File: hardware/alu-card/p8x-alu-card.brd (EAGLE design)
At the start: 160 x 100 mm, 77 parts, among them J1 FABC96R, U1 74HCT377, U10 74HCT181, U11 74HCT182, U12 74HCT157, U13 74HCT157, U14 74HCT157, U15 74HCT157, U16 74HCT244, U17 FLAGS, U18 74HCT260, U19 74HCT08, U2 74HCT244, U20 74HCT138, U21 74HCT138, U22 74HCT157, U23 74HCT244, U24 74HCT32, U25 74HCT00, U26 74HCT74, U27 74HCT260, U28 74HCT157, U29 74HCT157, U3 74HCT377, U30 74HCT157, U31 74HCT08, U32 74HCT157, U33 74HCT157, U34 74HCT86, U35 74HCT08, U4 74HCT244, U5 74HCT377, U6 74HCT244, U7 74HCT377, U8 74HCT244, U9 74HCT181

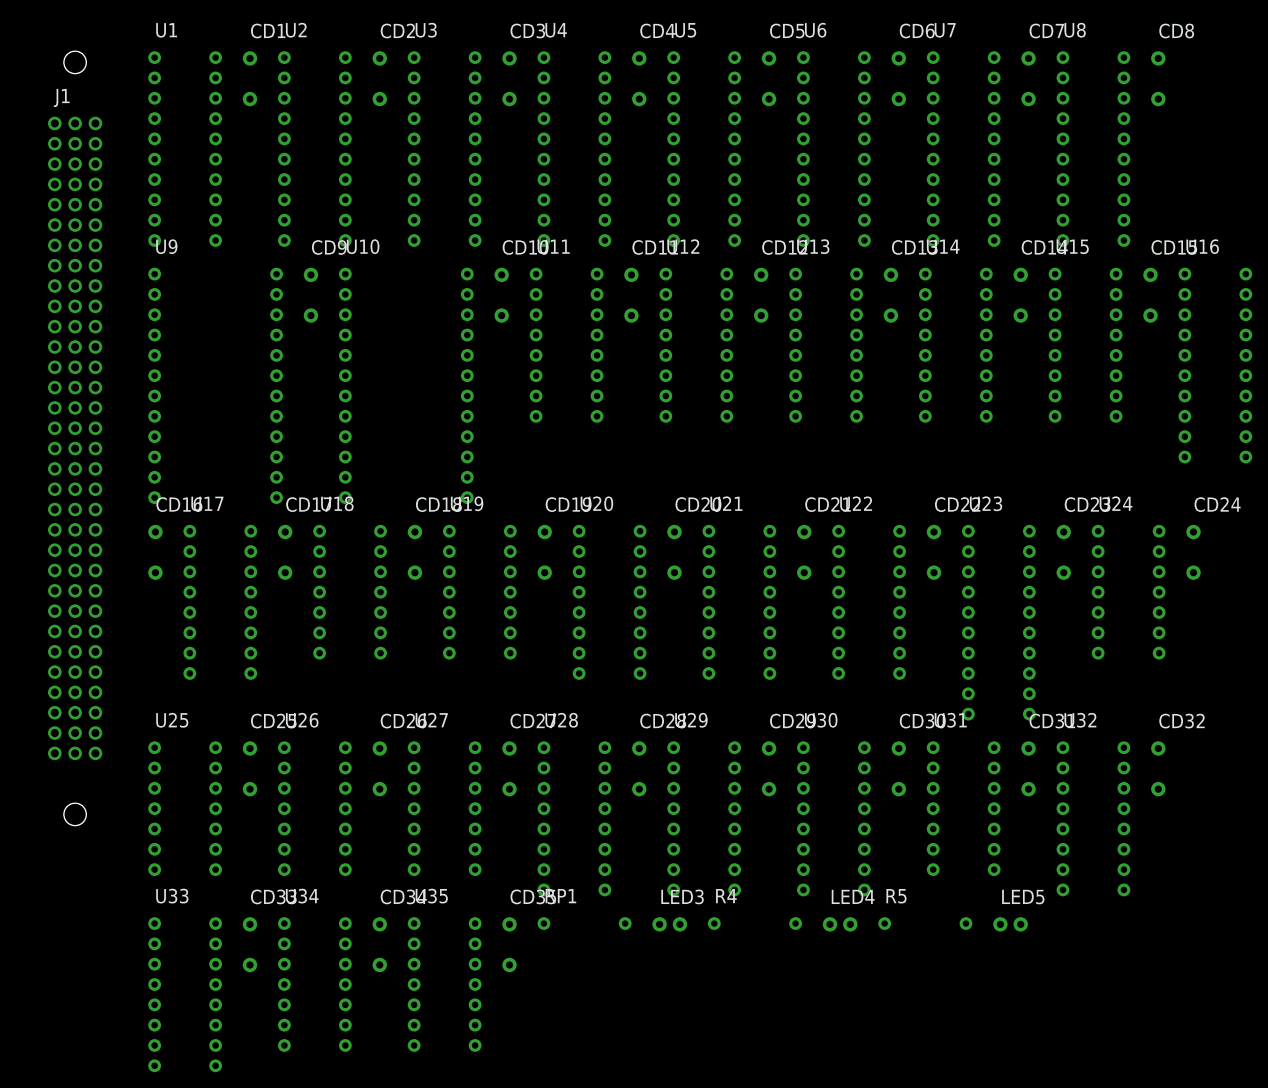
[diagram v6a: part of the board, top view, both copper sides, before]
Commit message: feat(hardware): use con-vg DIN 41612 footprints (MABC96R card / FABC96S backplane)
Replace the hand-rolled DIN96/DIN96C connector packages with the real Eagle
con-vg DIN 41612 footprints (geometry baked into the generator so it stays
self-contained): card edge = MABC96R (male right-angle), backplane = FABC96S
(female vertical) — both A/B/C @ 2.54mm, drill 0.9144, two M2.5 mounting holes
at y=+/-45. Card value -> MABC96R; pin->pad names unchanged (A1..C32) so the
netlist is intact.

con-vg centres the pad field on the element origin, so the backplane (hand-
placed/routed) was re-derived: slots dropped to y=54.6 to centre the pin field
on the 109mm board (pads now on-board), bus traces re-routed to the new A/B/C
columns (element at sx(i)-2.54). Cards auto-adapt via fp_box. All 8 boards
validate (0 errors).

Known: 3 placement-overlap WARNINGS on the backplane (power-LED resistor; CT2/RT1
clock terminators, both DNP) where the taller connector crowds the top/bottom
strips — to clear during the Fusion placement pass.

Co-Authored-By: Claude Opus 4.8 <noreply@anthropic.com>
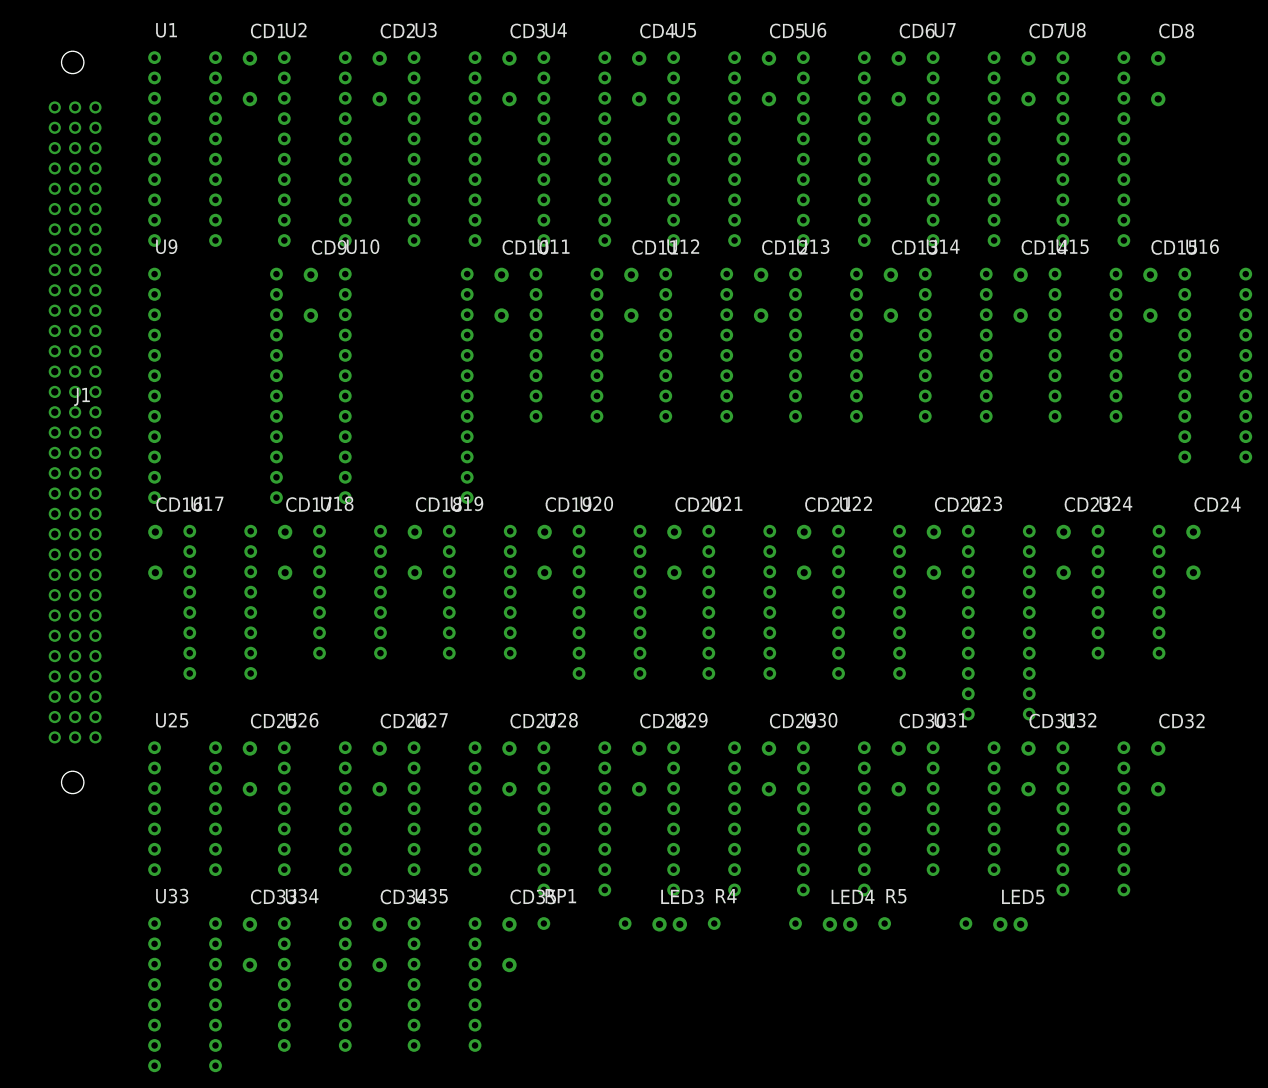
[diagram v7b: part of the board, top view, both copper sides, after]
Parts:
- J1: value FABC96R -> MABC96R; device p8x:DIN96C -> p8x:MABC96R
- moved J1 37.5 mm to (193.3, 49.6)

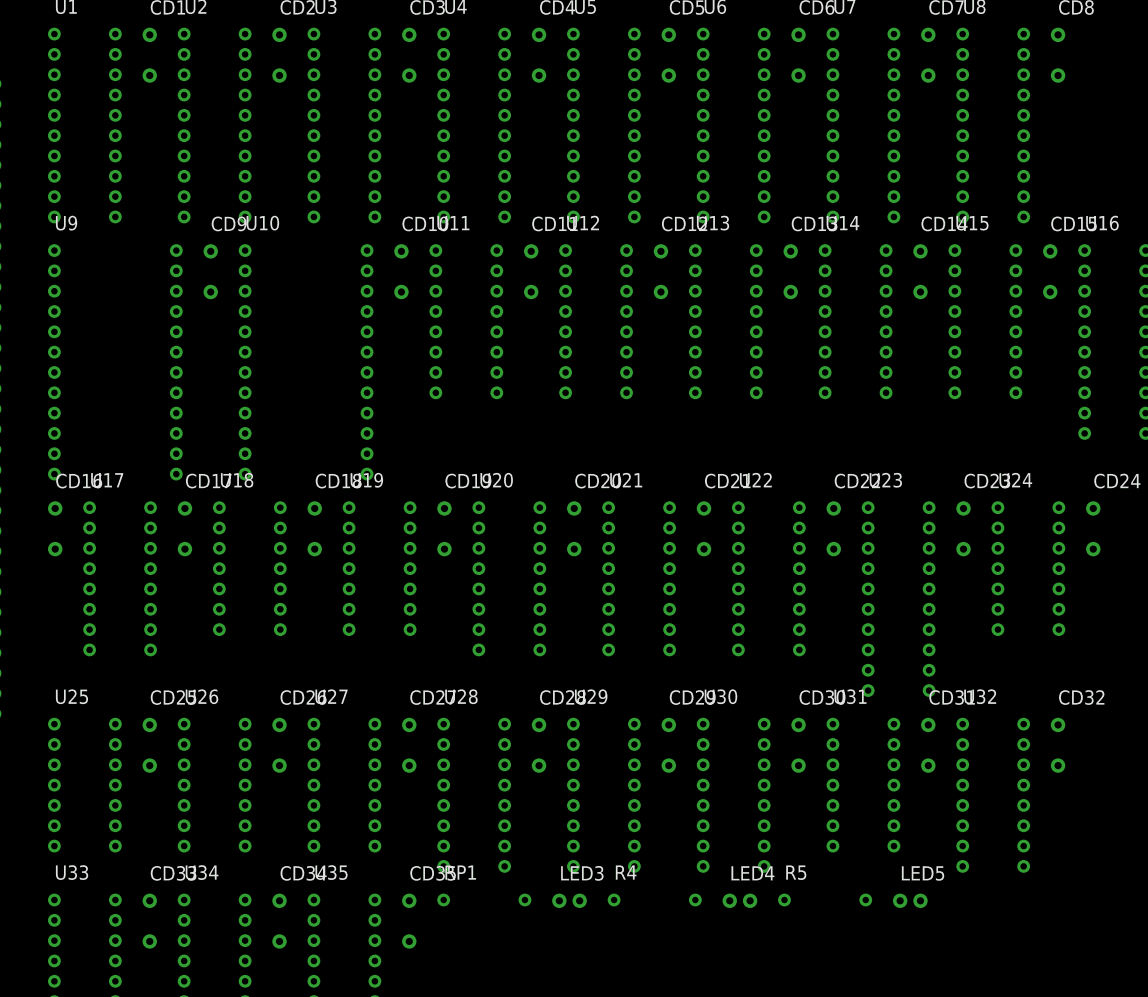
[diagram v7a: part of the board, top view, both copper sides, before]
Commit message: feat(hardware): 100nF bypass caps to 0.1" lead pitch on all boards
The 100nF ceramic-disc decoupling/bypass caps used the shared C_DISC footprint
at 0.2" (5.08mm) lead spacing. The parts being sourced are 0.1" (2.54mm) pitch,
so retarget just those caps:

- Add a C_DISC1 footprint (pad 2 at y=-2.54) and a CAP1 device that reuses the
  CAP schematic symbol art but points at C_DISC1.
- Route the 100nF parts to CAP1: per-IC decoupling (CDn), the placement-flow
  copies, and the backplane per-slot caps C1-C10.
- Leave C_DISC (0.2") for the parts that still use it: the 1uF caps, the 150pF
  clock terminators (CT1/CT2), and the XTAL32 placeholder.

Regenerated all 8 boards (.sch/.brd/-full.brd) and the schematic PDFs; the
narrower pad field also relieves the backplane connector clearance. Validation:
0 errors on all boards.

Co-Authored-By: Claude Opus 4.8 <noreply@anthropic.com>
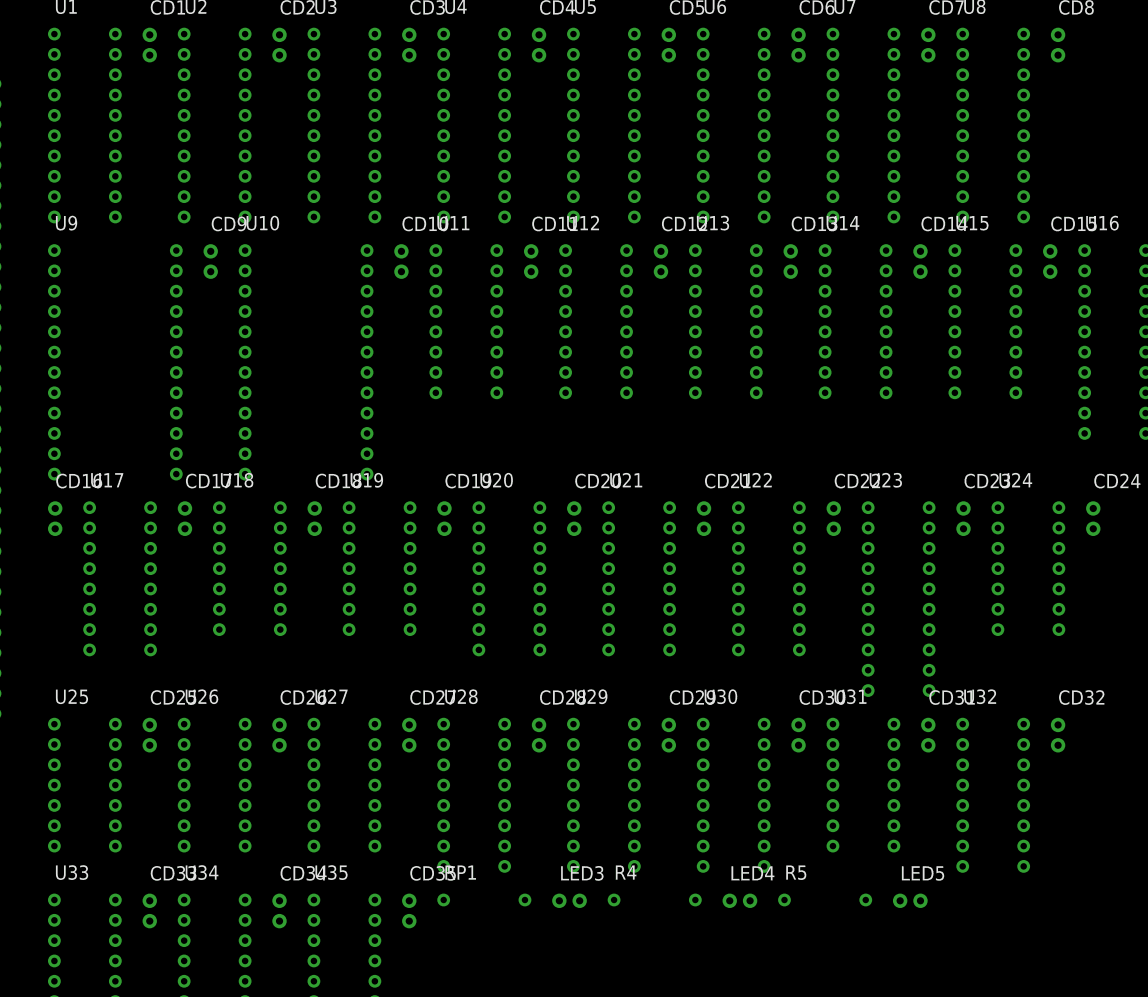
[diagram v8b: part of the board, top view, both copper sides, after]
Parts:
- CD1, CD10, CD11, CD12, CD13, CD14, CD15, CD16, CD17, CD18, CD19, CD2, CD20, CD21, CD22, CD23, CD24, CD25, CD26, CD27, CD28, CD29, CD3, CD30, CD31, CD32, CD33, CD34, CD35, CD4, CD5, CD6, CD7, CD8, CD9: device p8x:C_DISC -> p8x:C_DISC1
